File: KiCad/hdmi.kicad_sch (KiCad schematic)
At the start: 34 parts, among them J25 HDMI_A, Q1 2N7002, Q2 2N7002, Q3 2N7002, U20 H5VU25U, U21 H5VU25U

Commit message: Finish fixing footprints
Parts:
- renumbered C324 to C323, C325 to C324, C326 to C325, C327 to C326, C328 to C327, C329 to C328, C330 to C329, C323 to C330, D38 to D34, D37 to D35, J25 to J26, Q3 to Q1, Q1 to Q3, R207 to R201, R208 to R202, R209 to R203, R210 to R204, R211 to R205, R212 to R206, R213 to R207, R214 to R208, R215 to R209, R216 to R210, R202 to R211, R203 to R212, R205 to R213, R206 to R214, R204 to R215, U20 to U38, U21 to U39

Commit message: Re-annotate schematic
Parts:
- renumbered C323 to C333, C324 to C334, C325 to C335, C326 to C336, C327 to C337, C328 to C338, C329 to C339, C330 to C340, C331 to C341, J26 to J24, R201 to R194, R202 to R195, R203 to R196, R204 to R197, R205 to R198, R206 to R199, R207 to R200, R208 to R201, R209 to R202, R210 to R203, R211 to R204, R212 to R205, R213 to R206, R214 to R207, R215 to R208

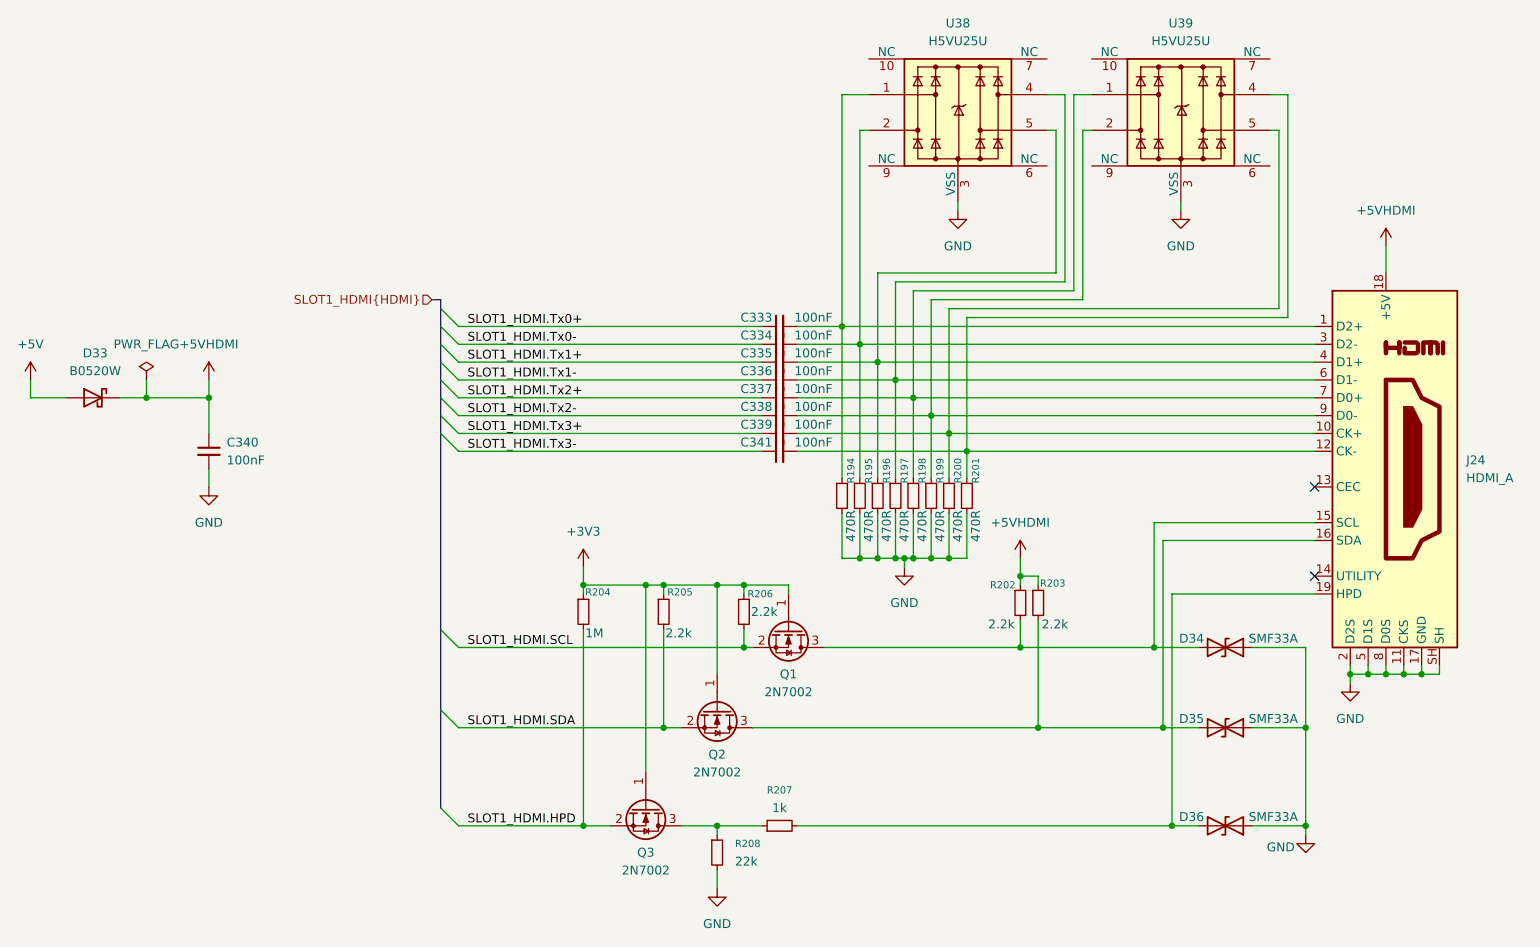
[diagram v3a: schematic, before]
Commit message: Move HDMI to module sheet
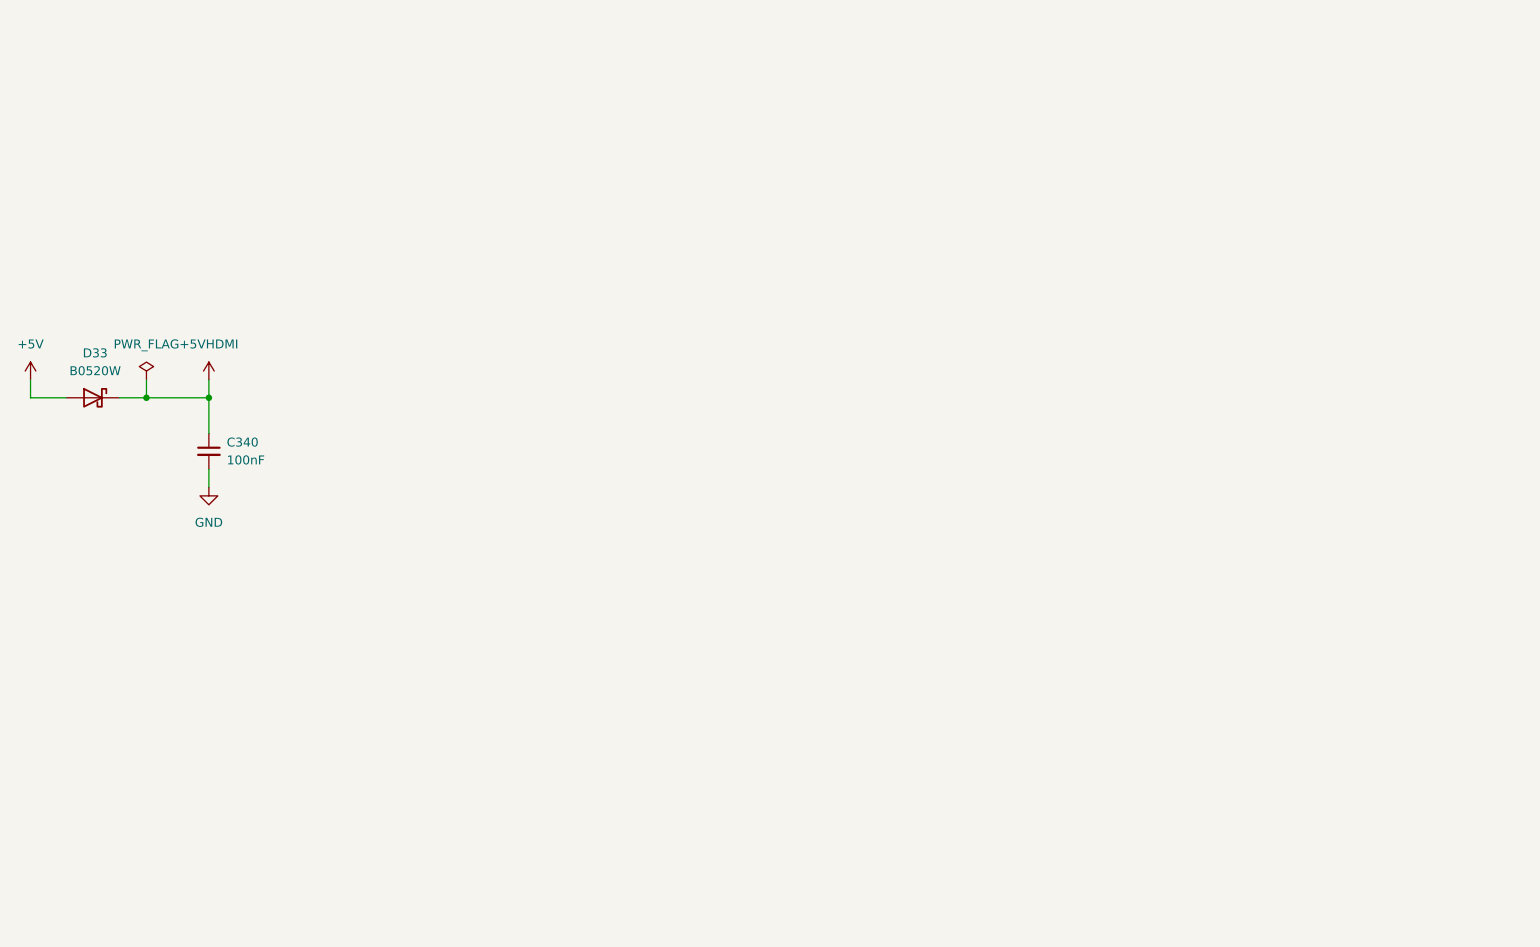
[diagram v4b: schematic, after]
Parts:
- removed C333, C334, C335, C336, C337, C338, C339, C341: 100nF, Capacitor_SMD:C_0402_1005Metric, symbol Device:C_Small
- removed D34, D35, D36: SMF33A, Diode_SMD:D_SOD-123F, symbol Device:D_TVS
- removed J24: HDMI_A, Connector_Video:HDMI_A_Molex_208658-1001_Horizontal, symbol Connector:HDMI_A
- removed Q1, Q2, Q3: 2N7002, Package_TO_SOT_SMD:SOT-23, symbol Transistor_FET:Q_NMOS_GSD
- removed R194, R195, R196, R197, R198, R199, R200, R201: 470R, Resistor_SMD:R_0402_1005Metric, symbol Device:R_Small
- removed R202, R203, R205, R206: 2.2k, Resistor_SMD:R_0402_1005Metric, symbol Device:R_Small
- removed R204: 1M, Resistor_SMD:R_0402_1005Metric, symbol Device:R_Small
- removed R207: 1k, Resistor_SMD:R_0805_2012Metric, symbol Device:R_Small
- removed R208: 22k, Resistor_SMD:R_0402_1005Metric, symbol Device:R_Small
- removed U38, U39: H5VU25U, Package_DFN_QFN:Diodes_UDFN-10_1.0x2.5mm_P0.5mm, symbol Power_Protection:D3V3XA4B10LP
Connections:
- no-connect marks 2 -> 0
